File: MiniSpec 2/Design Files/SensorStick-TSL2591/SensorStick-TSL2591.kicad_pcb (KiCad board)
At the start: 2 copper layers, 14 x 25 mm, 6 parts, among them J1 TSM-104-02-S-DV-P-TR, U1 TSL25721FN

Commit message: working on TSL2591 board
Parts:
- removed U1: TSL25721FN, KiCAD Part Library:TSL2752
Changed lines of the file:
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@@
   (net 3 "SDA")
   (net 4 "SCL")
-  (net 5 "Net-(R3-Pad2)")
-  (net 6 "unconnected-(U1-Pad4)")
-  (net 7 "Net-(IC1-Pad2)")
+  (net 5 "Net-(R2-Pad2)")
   (footprint "SamacSys_Parts:TSM-104-YY-ZZZ-DV-P-TR" (layer "F.Cu")
     (at 137.81 74.475)
@@
       (net 2 "+3V3") (pintype "passive"))
     (pad "2" smd roundrect locked (at 1.4 0) (size 1.25 1.75) (layers "F.Cu" "F.Paste" "F.Mask") (roundrect_rratio 0.2)
-      (net 7 "Net-(IC1-Pad2)") (pintype "passive"))
+      (net 5 "Net-(R2-Pad2)") (pintype "passive"))
     (model "${KISYS3DMOD}/Resistor_SMD.3dshapes/R_1206_3216Metric.wrl"
       (offset (xyz 0 0 0))
@@
       (rotate (xyz 0 0 0))
     )
-  )
-  (footprint "KiCAD Part Library:TSL2752" (layer "F.Cu")
-    (at 137.0875 68.025 90)
-    (property "Arrow Part Number" "TSL25721FN")
-    (property "Arrow Price/Stock" "https://www.arrow.com/en/products/tsl25721fn/ams-ag?region=nac")
-    (property "Description" "Light to Digital Converters ALS, I2C Vbus= VDD Interface")
-    (property "Height" "")
-    (property "Manufacturer_Name" "ams")
-    (property "Manufacturer_Part_Number" "TSL25721FN")
-    (property "Mouser Part Number" "985-TSL25721FN")
-    (property "Mouser Price/Stock" "https://www.mouser.co.uk/ProductDetail/ams/TSL25721FN?qs=ECv0MKUHA8GP%252Bsx2cFEj1g%3D%3D")
-    (property "Sheetfile" "SensorStick-TSL2572.kicad_sch")
-    (property "Sheetname" "")
-    (attr smd)
-    (fp_text reference "U1" (at 0 -5.08 90 unlocked) (layer "F.SilkS") hide
-      (effects (font (size 1 1) (thickness 0.15)))
-    )
-    (fp_text value "TSL25721FN" (at 0 -10.16 90 unlocked) (layer "F.Fab")
-      (effects (font (size 1 1) (thickness 0.15)))
-    )
-    (fp_text user "${REFERENCE}" (at 0 -7.62 90 unlocked) (layer "F.Fab")
-      (effects (font (size 1 1) (thickness 0.15)))
-    )
-    (pad "1" smd rect (at 0.6 0.2 90) (size 1.2 0.35) (layers "F.Cu" "F.Paste" "F.Mask")
-      (net 2 "+3V3") (pinfunction "VDD") (pintype "passive"))
-    (pad "2" smd roundrect (at 0.6 0.85 90) (size 1.2 0.35) (layers "F.Cu" "F.Paste" "F.Mask") (roundrect_rratio 0.25)
-      (net 4 "SCL") (pinfunction "SCL") (pintype "passive"))
-    (pad "3" smd roundrect (at 0.6 1.5 90) (size 1.2 0.35) (layers "F.Cu" "F.Paste" "F.Mask") (roundrect_rratio 0.25)
-      (net 1 "GND") (pinfunction "GND") (pintype "passive"))
-    (pad "4" smd roundrect (at 2.1 1.5 90) (size 1.2 0.35) (layers "F.Cu" "F.Paste" "F.Mask") (roundrect_rratio 0.25)
-      (net 6 "unconnected-(U1-Pad4)") (pinfunction "NC") (pintype "no_connect"))
-    (pad "5" smd roundrect (at 2.1 0.85 90) (size 1.2 0.35) (layers "F.Cu" "F.Paste" "F.Mask") (roundrect_rratio 0.25)
-      (net 5 "Net-(R3-Pad2)") (pinfunction "INT") (pintype "passive"))
-    (pad "6" smd roundrect (at 2.1 0.2 90) (size 1.2 0.35) (layers "F.Cu" "F.Paste" "F.Mask") (roundrect_rratio 0.25)
-      (net 3 "SDA") (pinfunction "SDA") (pintype "passive"))
   )
   (gr_line (start 145 87) (end 131 87) (layer "Edge.Cuts") (width 0.05))
@@
   (segment (start 140.4 68.6) (end 141 68) (width 0.25) (layer "F.Cu") (net 4))
   (segment (start 141.6 68.2) (end 141 67.6) (width 0.25) (layer "F.Cu") (net 4))
-  (segment (start 139.1 63.8) (end 139.2 63.8) (width 0.25) (layer "F.Cu") (net 7))
-  (segment (start 139.4 63) (end 139 63.4) (width 0.25) (layer "F.Cu") (net 7))
+  (segment (start 139.1 63.8) (end 139.2 63.8) (width 0.25) (layer "F.Cu") (net 5))
+  (segment (start 139.4 63) (end 139 63.4) (width 0.25) (layer "F.Cu") (net 5))
   (zone (net 1) (net_name "GND") (layer "F.Cu") (hatch edge 0.508)
     (connect_pads (clearance 0.508))

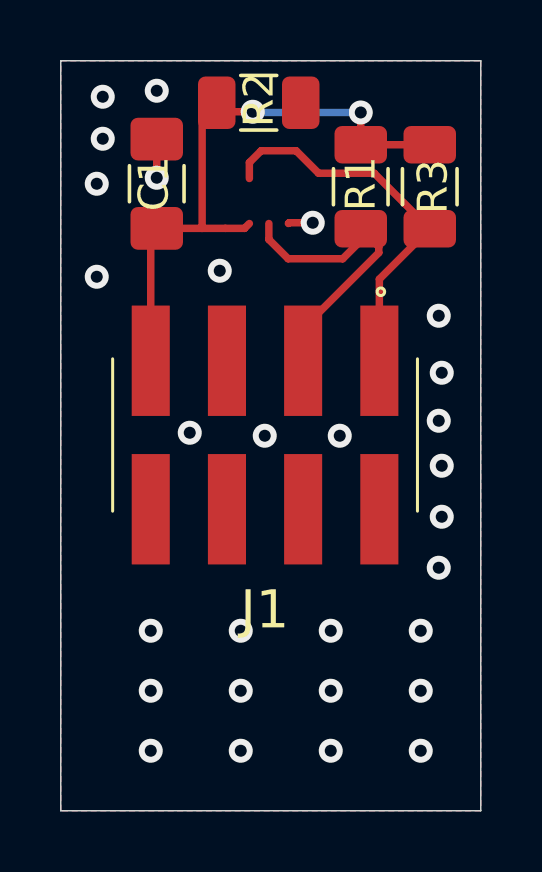
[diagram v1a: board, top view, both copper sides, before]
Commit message: added phone jack port for 25mm tube base
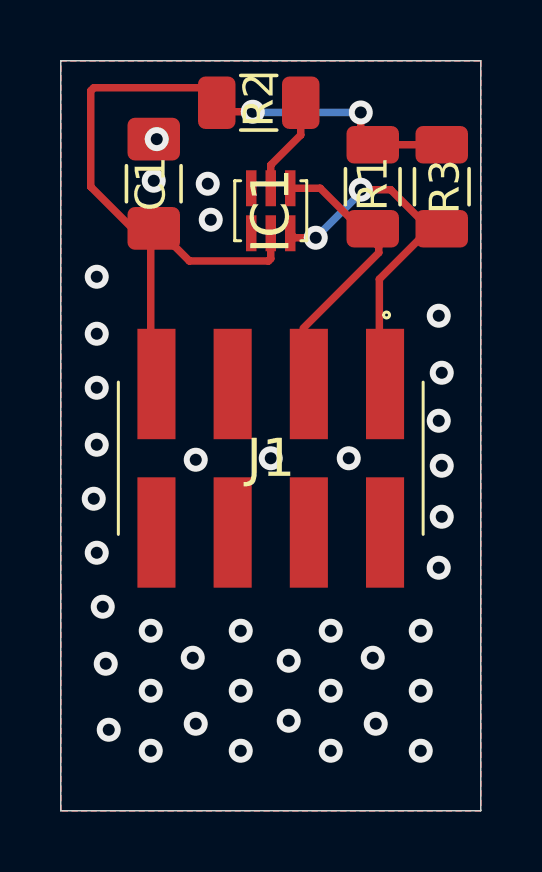
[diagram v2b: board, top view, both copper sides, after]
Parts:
- added IC1: TSL25913FN, BinomicaLabs:TSL25911FN, F.Cu at (138.0, 67.0)
- J1: footprint SamacSys_Parts:TSM-104-YY-ZZZ-DV-P-TR -> BinomicaLabs:TSM-104-YY-ZZZ-DV-P-TR
- moved J1 0.80 mm to (138.0, 75.2)
- moved R1 0.40 mm to (141.4, 66.2)
- moved R3 0.40 mm to (143.7, 66.2)
- moved C1 0.10 mm to (134.1, 66.1)
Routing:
- net +3V3: track 22.3 -> 28.3 mm
- net SCL: track 11.4 -> 7.52 mm
- net Net-(IC1-Pad2): track 0.67 -> 3.26 mm
- net GND: track 2.53 -> 0.00 mm, vias 29 -> 40
- net SDA: track 12.6 -> 10.8 mm, vias 0 -> 2
